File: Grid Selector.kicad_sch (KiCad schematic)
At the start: 92 parts, among them SW1 MX_SW_HS, SW10 MX_SW_HS, SW11 MX_SW_HS, SW12 MX_SW_HS, SW13 MX_SW_HS, SW14 MX_SW_HS, SW15 MX_SW_HS, SW16 MX_SW_HS, SW17 MX_SW_HS, SW18 MX_SW_HS, SW19 MX_SW_HS, SW2 MX_SW_HS, SW20 MX_SW_HS, SW21 MX_SW_HS, SW22 MX_SW_HS, SW23 MX_SW_HS, SW24 MX_SW_HS, SW25 MX_SW_HS, SW26 MX_SW_HS, SW27 MX_SW_HS, SW28 MX_SW_HS, SW29 MX_SW_HS, SW3 MX_SW_HS, SW30 MX_SW_HS, SW4 MX_SW_HS, SW5 MX_SW_HS, SW6 MX_SW_HS, SW7 MX_SW_HS, SW8 MX_SW_HS, SW9 MX_SW_HS, U1 Pico

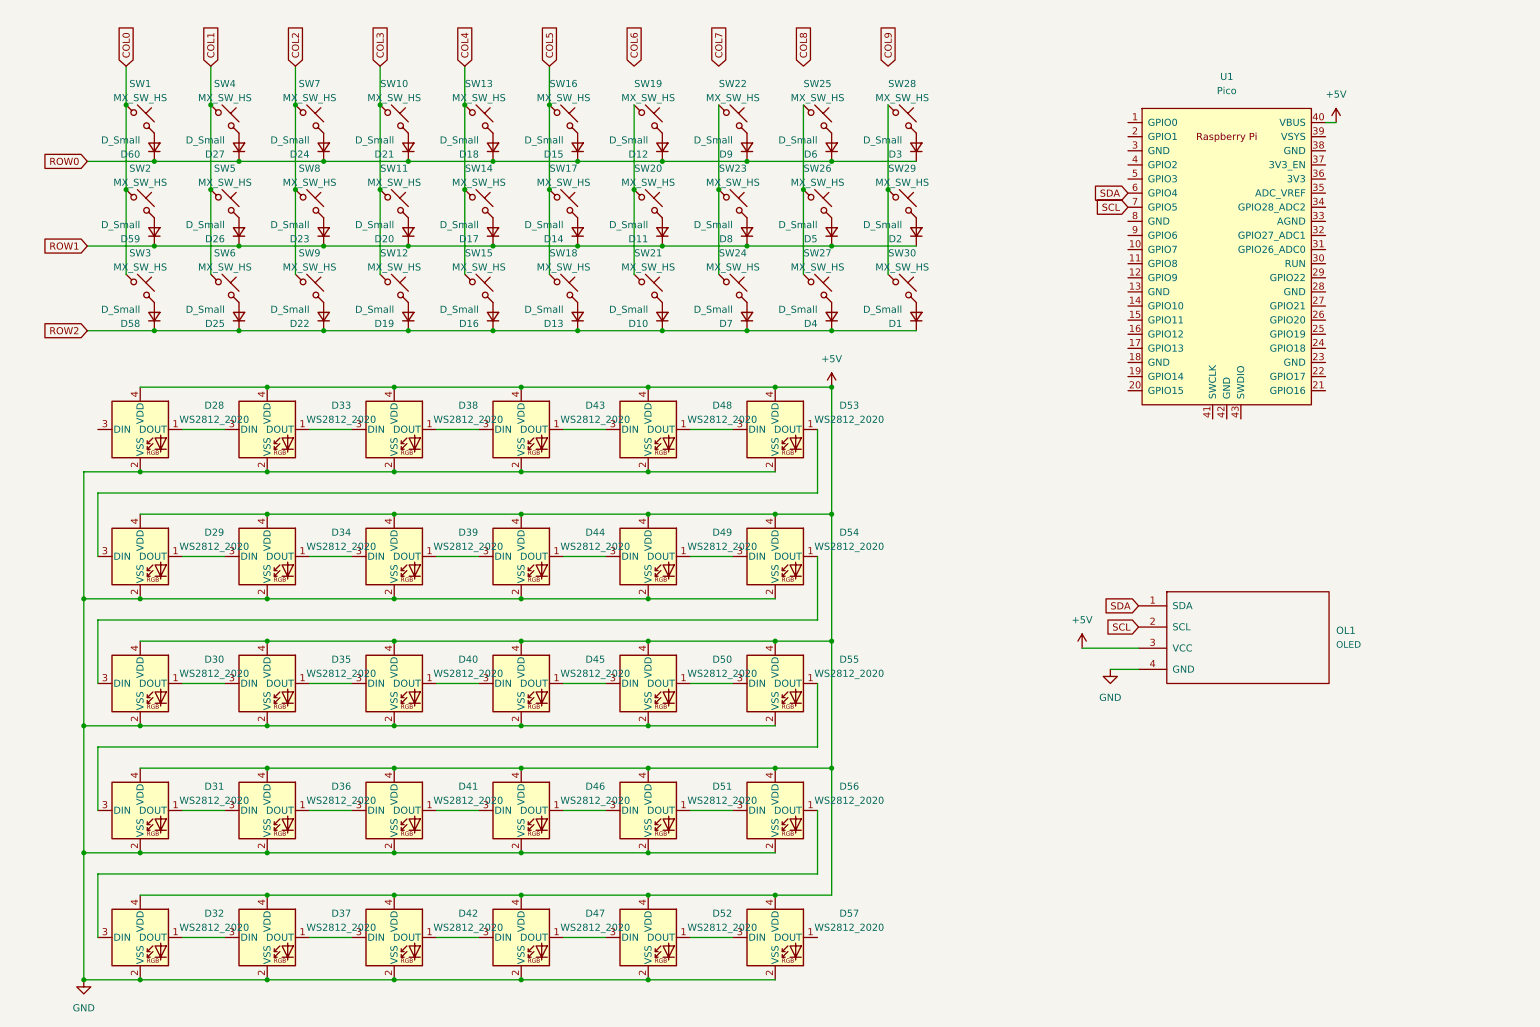
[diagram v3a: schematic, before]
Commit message: added current limiting resistors to led chain
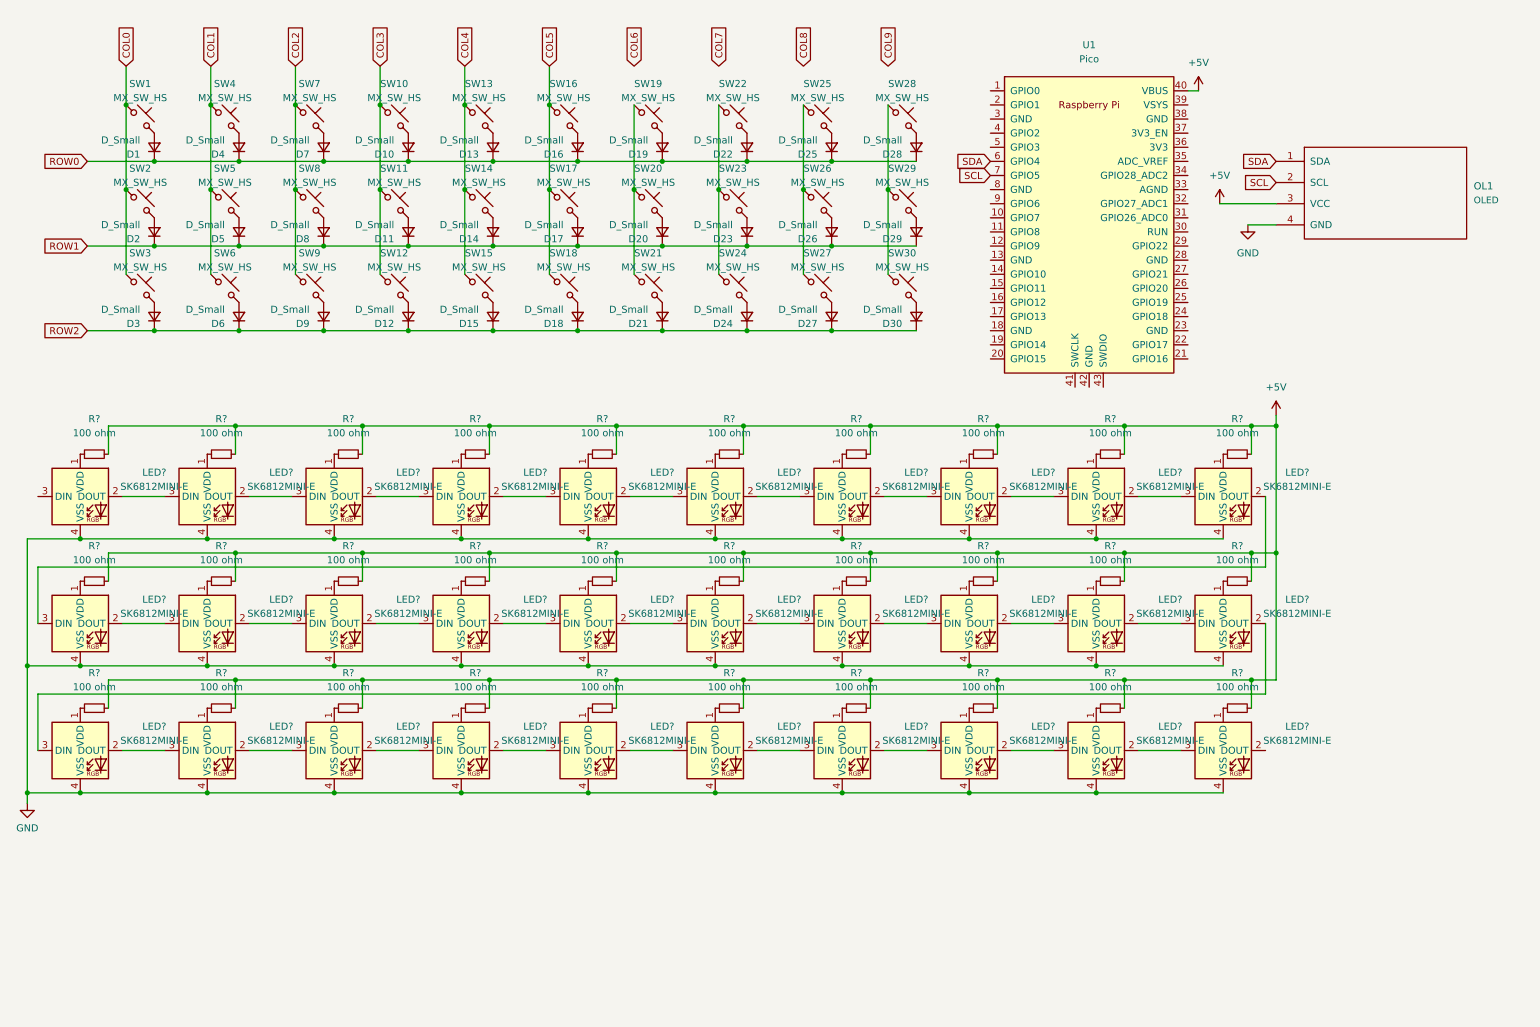
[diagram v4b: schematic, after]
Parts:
- removed D28, D29, D30, D31, D32, D33, D34, D35, D36, D37, D38, D39, D40, D41, D42, D43, D44, D45, D46, D47, D48, D49, D50, D51, D52, D53, D54, D55, D56, D57: WS2812_2020, marbastlib-various:LED_WS2812_2020, symbol marbastlib-various:WS2812_2020
- added LED? (x30): SK6812MINI-E, marbastlib-various:LED_6028R, symbol marbastlib-various:SK6812MINI-E
- added R? (x30): 100 ohm, symbol Device:R_Small
- renumbered D60 to D1, D21 to D10, D20 to D11, D19 to D12, D18 to D13, D17 to D14, D16 to D15, D15 to D16, D14 to D17, D13 to D18, D12 to D19, D59 to D2, D11 to D20, D10 to D21, D9 to D22, D8 to D23, D7 to D24, D6 to D25, D5 to D26, D4 to D27, D3 to D28, D2 to D29, D58 to D3, D1 to D30, D27 to D4, D26 to D5, D25 to D6, D24 to D7, D23 to D8, D22 to D9
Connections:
- net +5V: now also R?.2, R?.2, R?.2, R?.2, R?.2, R?.2, R?.2, R?.2, R?.2, R?.2, R?.2, R?.2, R?.2, R?.2, R?.2, R?.2, R?.2, R?.2, R?.2, R?.2, R?.2, R?.2, R?.2, R?.2, R?.2, R?.2, R?.2, R?.2, R?.2, R?.2
- net GND: now also LED?.4 (VSS), LED?.4 (VSS), LED?.4 (VSS), LED?.4 (VSS), LED?.4 (VSS), LED?.4 (VSS), LED?.4 (VSS), LED?.4 (VSS), LED?.4 (VSS), LED?.4 (VSS), LED?.4 (VSS), LED?.4 (VSS), LED?.4 (VSS), LED?.4 (VSS), LED?.4 (VSS), LED?.4 (VSS), LED?.4 (VSS), LED?.4 (VSS), LED?.4 (VSS), LED?.4 (VSS), LED?.4 (VSS), LED?.4 (VSS), LED?.4 (VSS), LED?.4 (VSS), LED?.4 (VSS), LED?.4 (VSS), LED?.4 (VSS), LED?.4 (VSS), LED?.4 (VSS), LED?.4 (VSS)
- new net: LED?.1 (VDD), R?.1 (x30)
- new net: LED?.2 (DOUT), LED?.3 (DIN) (x29)
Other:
- moved on the sheet: OL1, U1

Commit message: routed switch matrix and led chain
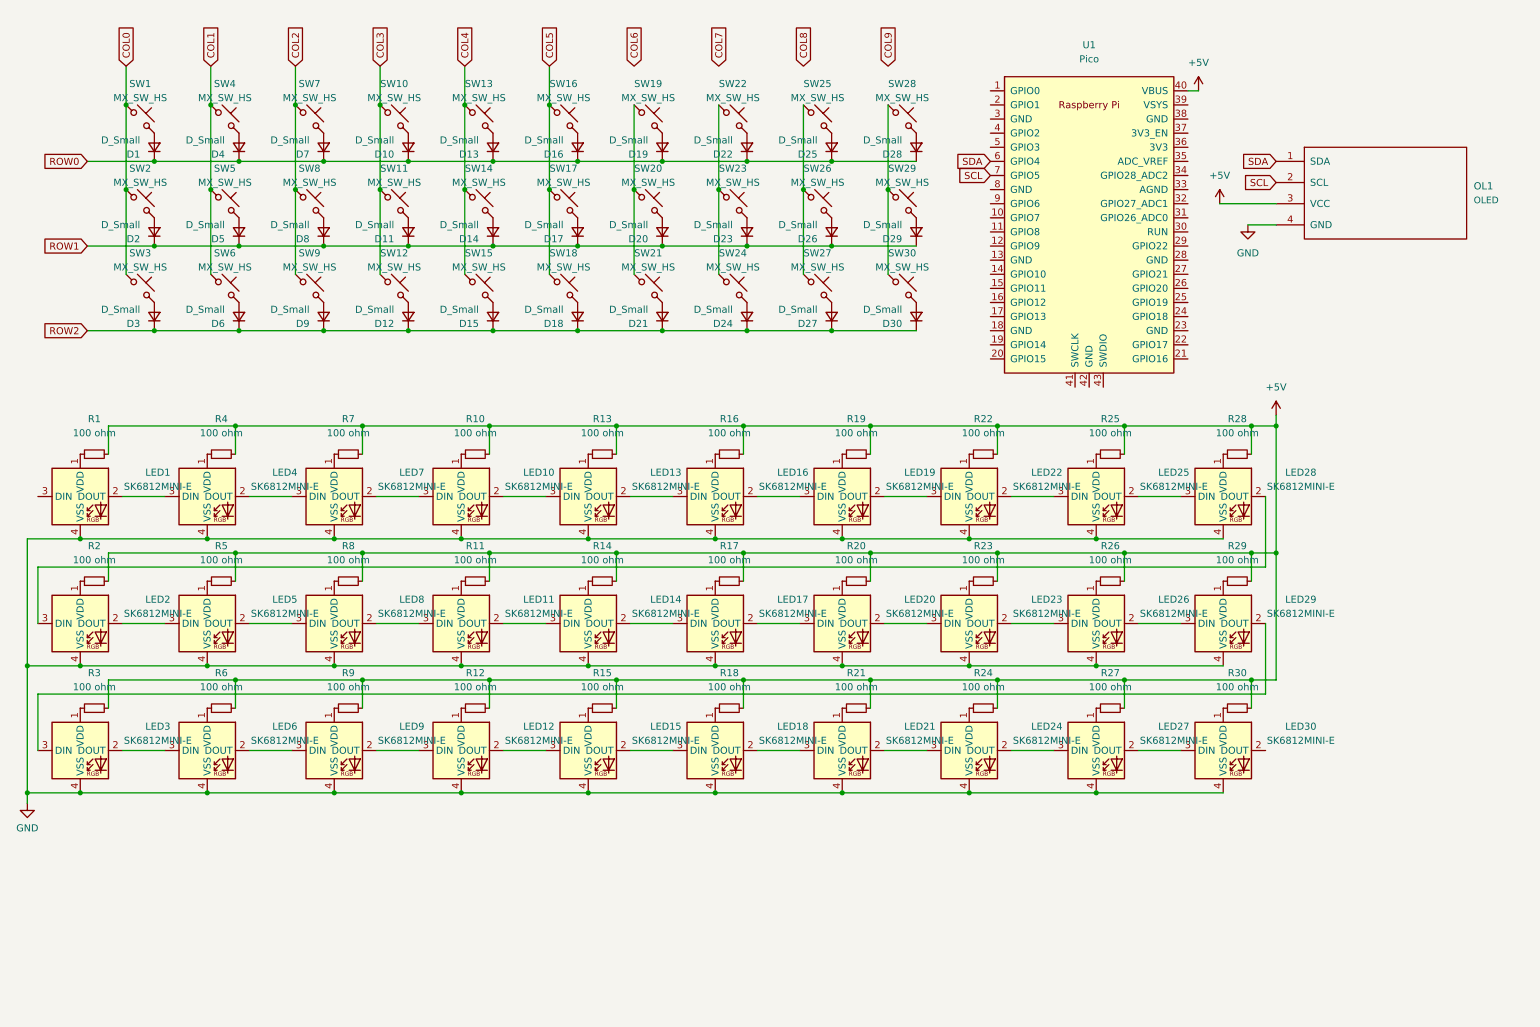
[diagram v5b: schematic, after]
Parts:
- removed LED? (x30): SK6812MINI-E, marbastlib-various:LED_6028R, symbol marbastlib-various:SK6812MINI-E
- added LED1, LED10, LED11, LED12, LED13, LED14, LED15, LED16, LED17, LED18, LED19, LED2, LED20, LED21, LED22, LED23, LED24, LED25, LED26, LED27, LED28, LED29, LED3, LED30, LED4, LED5, LED6, LED7, LED8, LED9: SK6812MINI-E, marbastlib-various:LED_6028R, symbol marbastlib-various:SK6812MINI-E
- R1, R10, R11, R12, R13, R14, R15, R16, R17, R18, R19, R2, R20, R21, R22, R23, R24, R25, R26, R27, R28, R29, R3, R30, R4, R5, R6, R7, R8, R9: renamed from R?; footprint (none) -> Resistor_SMD:R_0805_2012Metric
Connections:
- net GND: now also LED1.4 (VSS), LED10.4 (VSS), LED11.4 (VSS), LED12.4 (VSS), LED13.4 (VSS), LED14.4 (VSS), LED15.4 (VSS), LED16.4 (VSS), LED17.4 (VSS), LED18.4 (VSS), LED19.4 (VSS), LED2.4 (VSS), LED20.4 (VSS), LED21.4 (VSS), LED22.4 (VSS), LED23.4 (VSS), LED24.4 (VSS), LED25.4 (VSS), LED26.4 (VSS), LED27.4 (VSS), LED28.4 (VSS), LED29.4 (VSS), LED3.4 (VSS), LED30.4 (VSS), LED4.4 (VSS), LED5.4 (VSS), LED6.4 (VSS), LED7.4 (VSS), LED8.4 (VSS), LED9.4 (VSS)
- net at R25.1: now also LED25.1 (VDD)
- net at R21.1: now also LED21.1 (VDD)
- net at R10.1: now also LED10.1 (VDD)
- net at R8.1: now also LED8.1 (VDD)
- net at R27.1: now also LED27.1 (VDD)
- net at R2.1: now also LED2.1 (VDD)
- net at R26.1: now also LED26.1 (VDD)
- net at R4.1: now also LED4.1 (VDD)
- net at R7.1: now also LED7.1 (VDD)
- net at R20.1: now also LED20.1 (VDD)
- net at R22.1: now also LED22.1 (VDD)
- net at R5.1: now also LED5.1 (VDD)
- net at R30.1: now also LED30.1 (VDD)
- net at R6.1: now also LED6.1 (VDD)
- net at R15.1: now also LED15.1 (VDD)
- net at R16.1: now also LED16.1 (VDD)
- net at R17.1: now also LED17.1 (VDD)
- net at R9.1: now also LED9.1 (VDD)
- net at R1.1: now also LED1.1 (VDD)
- net at R19.1: now also LED19.1 (VDD)
- net at R3.1: now also LED3.1 (VDD)
- net at R23.1: now also LED23.1 (VDD)
- net at R24.1: now also LED24.1 (VDD)
- net at R11.1: now also LED11.1 (VDD)
- net at R12.1: now also LED12.1 (VDD)
- net at R13.1: now also LED13.1 (VDD)
- net at R18.1: now also LED18.1 (VDD)
- net at R14.1: now also LED14.1 (VDD)
- net at R28.1: now also LED28.1 (VDD)
- net at R29.1: now also LED29.1 (VDD)
- new net: LED26.2 (DOUT), LED29.3 (DIN)
- new net: LED23.2 (DOUT), LED26.3 (DIN)
- new net: LED12.3 (DIN), LED9.2 (DOUT)
- new net: LED6.2 (DOUT), LED9.3 (DIN)
- new net: LED10.3 (DIN), LED7.2 (DOUT)
- new net: LED4.2 (DOUT), LED7.3 (DIN)
- new net: LED12.2 (DOUT), LED15.3 (DIN)
- new net: LED11.3 (DIN), LED8.2 (DOUT)
- new net: LED5.2 (DOUT), LED8.3 (DIN)
- new net: LED17.2 (DOUT), LED20.3 (DIN)
- new net: LED14.2 (DOUT), LED17.3 (DIN)
- new net: LED2.2 (DOUT), LED5.3 (DIN)
- new net: LED10.2 (DOUT), LED13.3 (DIN)
- new net: LED13.2 (DOUT), LED16.3 (DIN)
- new net: LED27.2 (DOUT), LED30.3 (DIN)
- new net: LED24.2 (DOUT), LED27.3 (DIN)
- new net: LED1.2 (DOUT), LED4.3 (DIN)
- new net: LED11.2 (DOUT), LED14.3 (DIN)
- new net: LED22.2 (DOUT), LED25.3 (DIN)
- new net: LED19.2 (DOUT), LED22.3 (DIN)
- new net: LED16.2 (DOUT), LED19.3 (DIN)
- new net: LED15.2 (DOUT), LED18.3 (DIN)
- new net: LED21.2 (DOUT), LED24.3 (DIN)
- new net: LED25.2 (DOUT), LED28.3 (DIN)
- new net: LED18.2 (DOUT), LED21.3 (DIN)
- new net: LED2.3 (DIN), LED28.2 (DOUT)
- new net: LED3.2 (DOUT), LED6.3 (DIN)
- new net: LED20.2 (DOUT), LED23.3 (DIN)
- new net: LED29.2 (DOUT), LED3.3 (DIN)

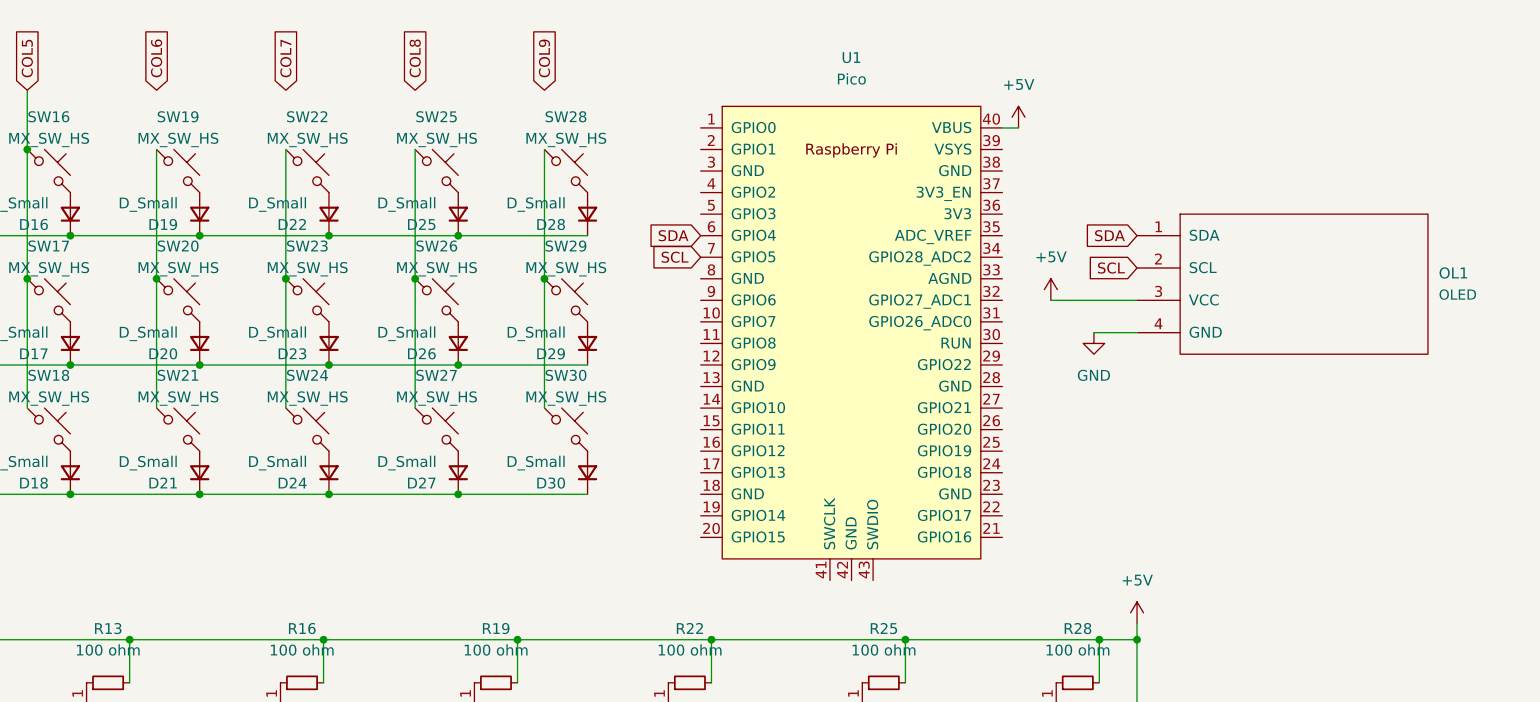
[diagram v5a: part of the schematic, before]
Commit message: connected switch matrix and led chain to pico
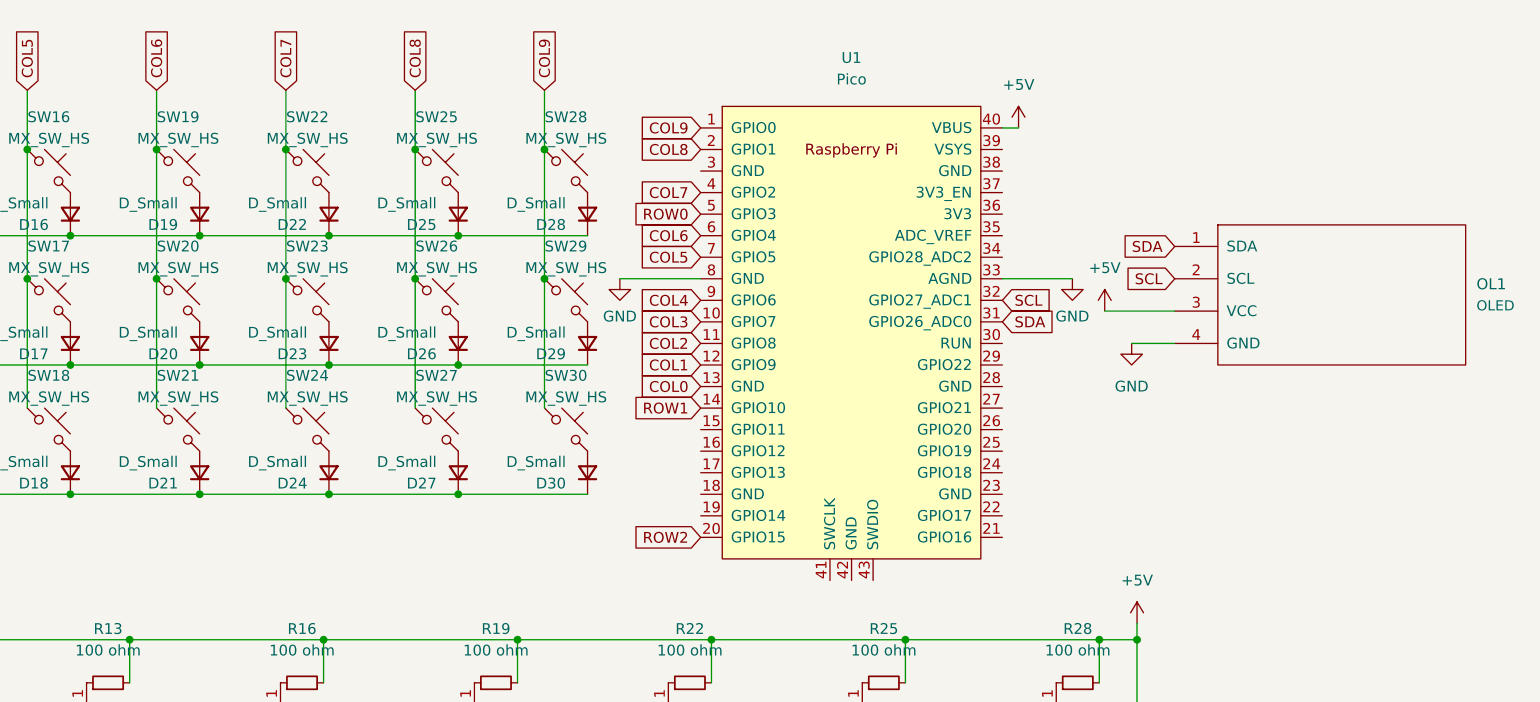
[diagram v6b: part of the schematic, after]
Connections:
- net COL0: now also U1.13 (GND)
- net COL1: now also U1.12 (GPIO9)
- net COL2: now also U1.11 (GPIO8)
- net COL3: now also U1.10 (GPIO7)
- net COL4: now also U1.9 (GPIO6)
- net COL5: now also U1.7 (GPIO5)
- net COL6: now also SW19.1, SW20.1, SW21.1, U1.6 (GPIO4)
- net COL7: now also SW22.1, SW23.1, SW24.1, U1.4 (GPIO2)
- net COL8: now also SW25.1, SW26.1, SW27.1, U1.2 (GPIO1)
- net COL9: now also SW28.1, SW29.1, SW30.1, U1.1 (GPIO0)
- net GND: now also U1.33 (AGND), U1.8 (GND)
- net ROW0: now also U1.5 (GPIO3)
- net ROW1: now also U1.14 (GPIO10)
- net ROW2: now also U1.20 (GPIO15)
- net SCL: now also U1.32 (GPIO27_ADC1); no longer U1.7 (GPIO5)
- net SDA: now also U1.31 (GPIO26_ADC0); no longer U1.6 (GPIO4)
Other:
- moved on the sheet: OL1
